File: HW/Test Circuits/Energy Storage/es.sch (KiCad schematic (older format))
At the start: 5 parts, among them J1 IN, J2 OUT

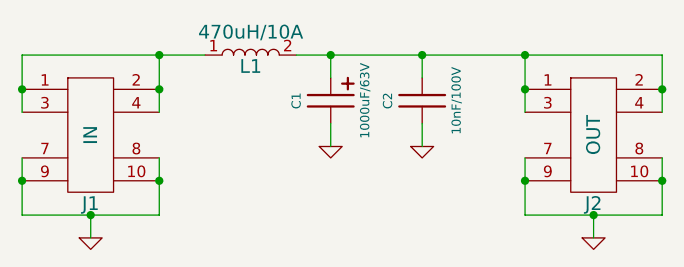
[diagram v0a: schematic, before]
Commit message: Motor Measurement circuit added (not complete)
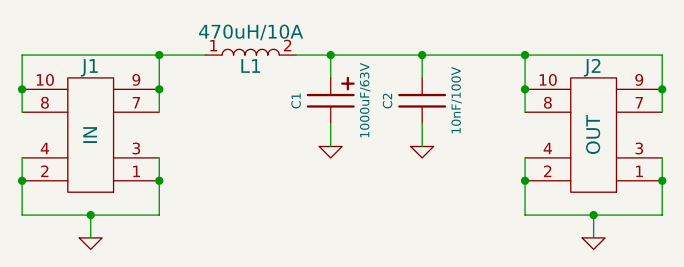
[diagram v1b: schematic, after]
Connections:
- net GND: now also J1.1, J1.2, J1.3, J1.4, J2.1, J2.2, J2.3, J2.4; no longer J1.10, J1.7, J1.8, J1.9, J2.10, J2.7, J2.8, J2.9
- new net: J1.10, J1.7, J1.8, J1.9, L1.1
- new net: C1.1, C2.1, J2.10, J2.7, J2.8, J2.9, L1.2
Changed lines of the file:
@@
 LIBS:contrib
 LIBS:valves
+LIBS:es-cache
 EELAYER 27 0
 EELAYER END
@@
 F 3 "" H 3700 3300 60  0000 C CNN
 	1    3700 3300
-	1    0    0    -1
+	-1   0    0    1
 $EndComp
 $Comp
@@
 F 3 "" H 5900 3300 60  0000 C CNN
 	1    5900 3300
-	1    0    0    -1
+	-1   0    0    1
 $EndComp
 Wire Wire Line
